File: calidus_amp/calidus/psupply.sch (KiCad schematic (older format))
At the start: 19 parts

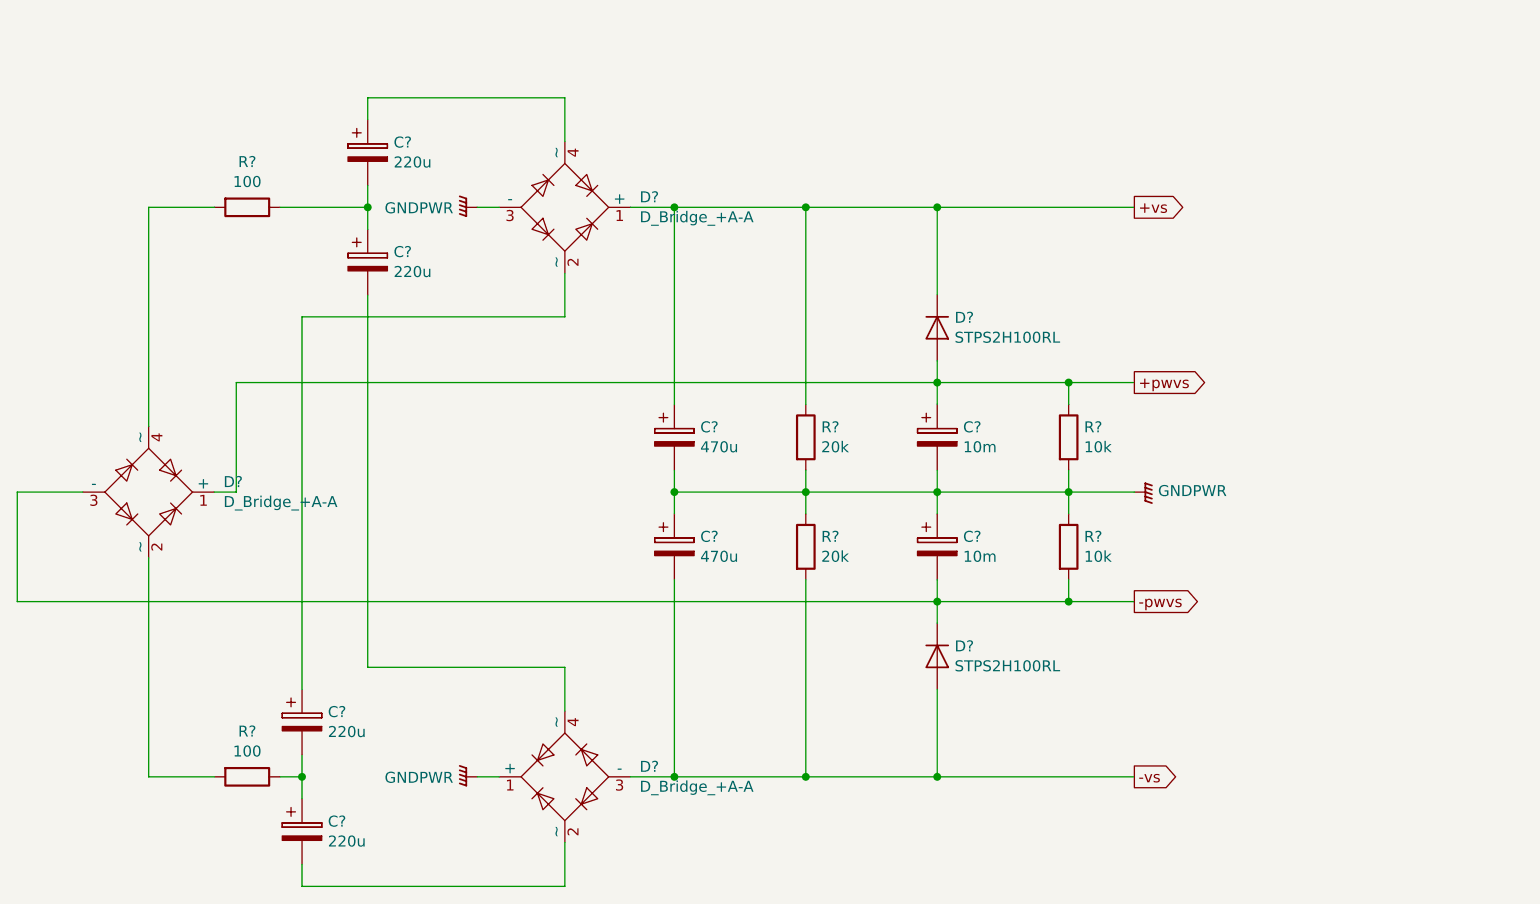
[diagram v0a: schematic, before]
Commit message: Upgraded power supply
Using new power supply design with 3pin linear regulator
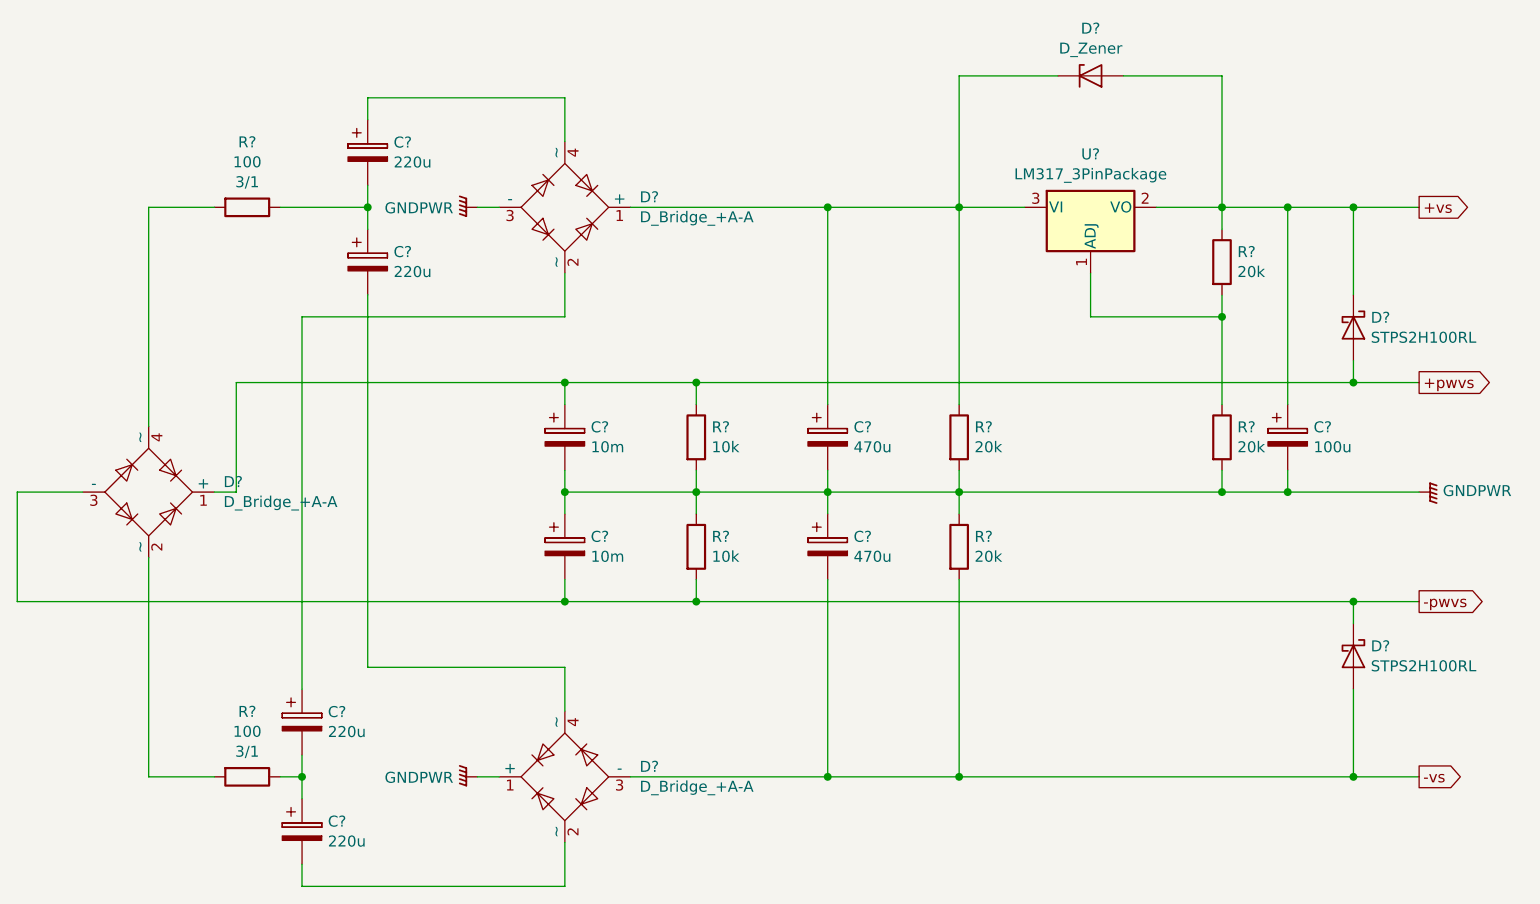
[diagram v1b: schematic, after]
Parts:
- removed D? (x2): STPS2H100RL, symbol Device:D
- removed R?: 100, symbol Device:R
- added C?: 100u, symbol Device:CP
- added D? (x2): STPS2H100RL, symbol Device:D_Schottky
- added D?: D_Zener, symbol Device:D_Zener
- added R? (x2): 20k, symbol Device:R
- added R?: 100, symbol Device:R
- added U?: LM317_3PinPackage, symbol Regulator_Linear:LM317_3PinPackage
- R?: Power (none) -> 3/1
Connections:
- net +pwvs: now also D?.2 (A)
- net +vs: now also C?.1, D?.1 (K), D?.2 (A), R?.1, U?.2 (VO); no longer C?.1, D?.1 (+), R?.1
- net -pwvs: now also D?.1 (K)
- net -vs: now also D?.2 (A)
- net GNDPWR: now also C?.2, R?.2
- net at D?.4 (~~): now also R?.2
- net at C?.1, C?.2: now also R?.1
- new net: C?.1, D?.1 (+), D?.1 (K), R?.1, U?.3 (VI)
- new net: R?.1, R?.2, U?.1 (ADJ)
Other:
- moved on the sheet: C?, R?

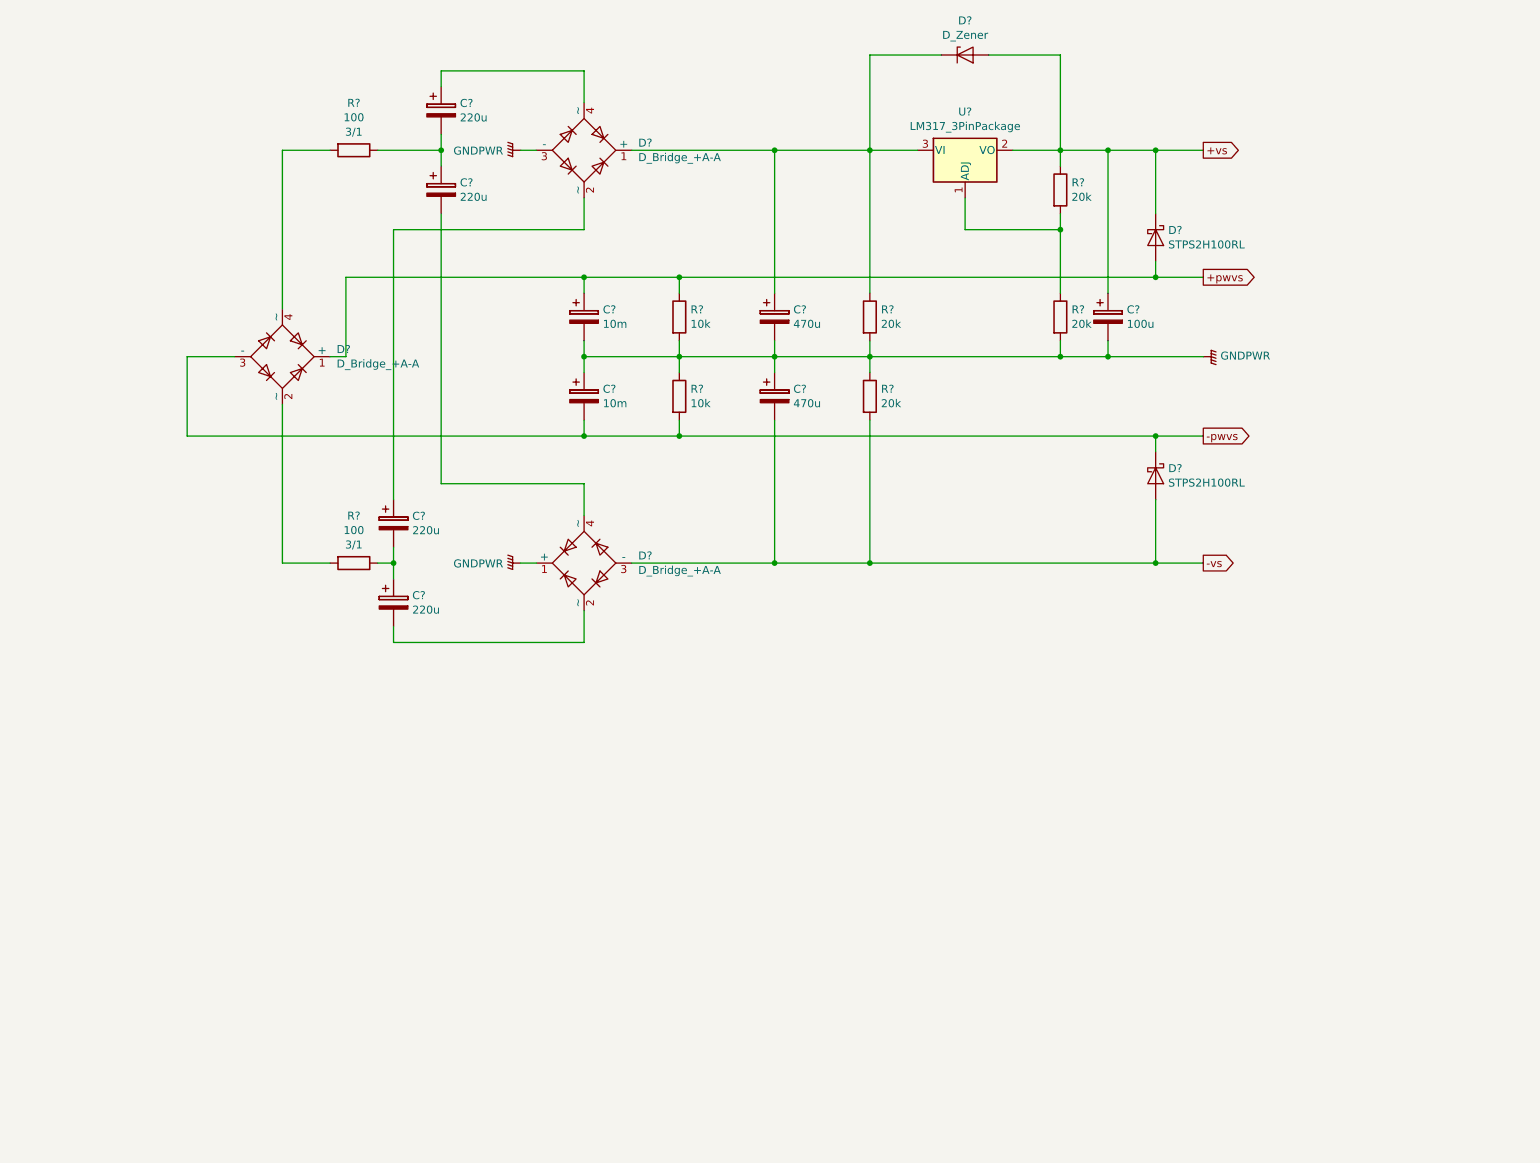
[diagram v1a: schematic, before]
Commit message: Update of the schematic
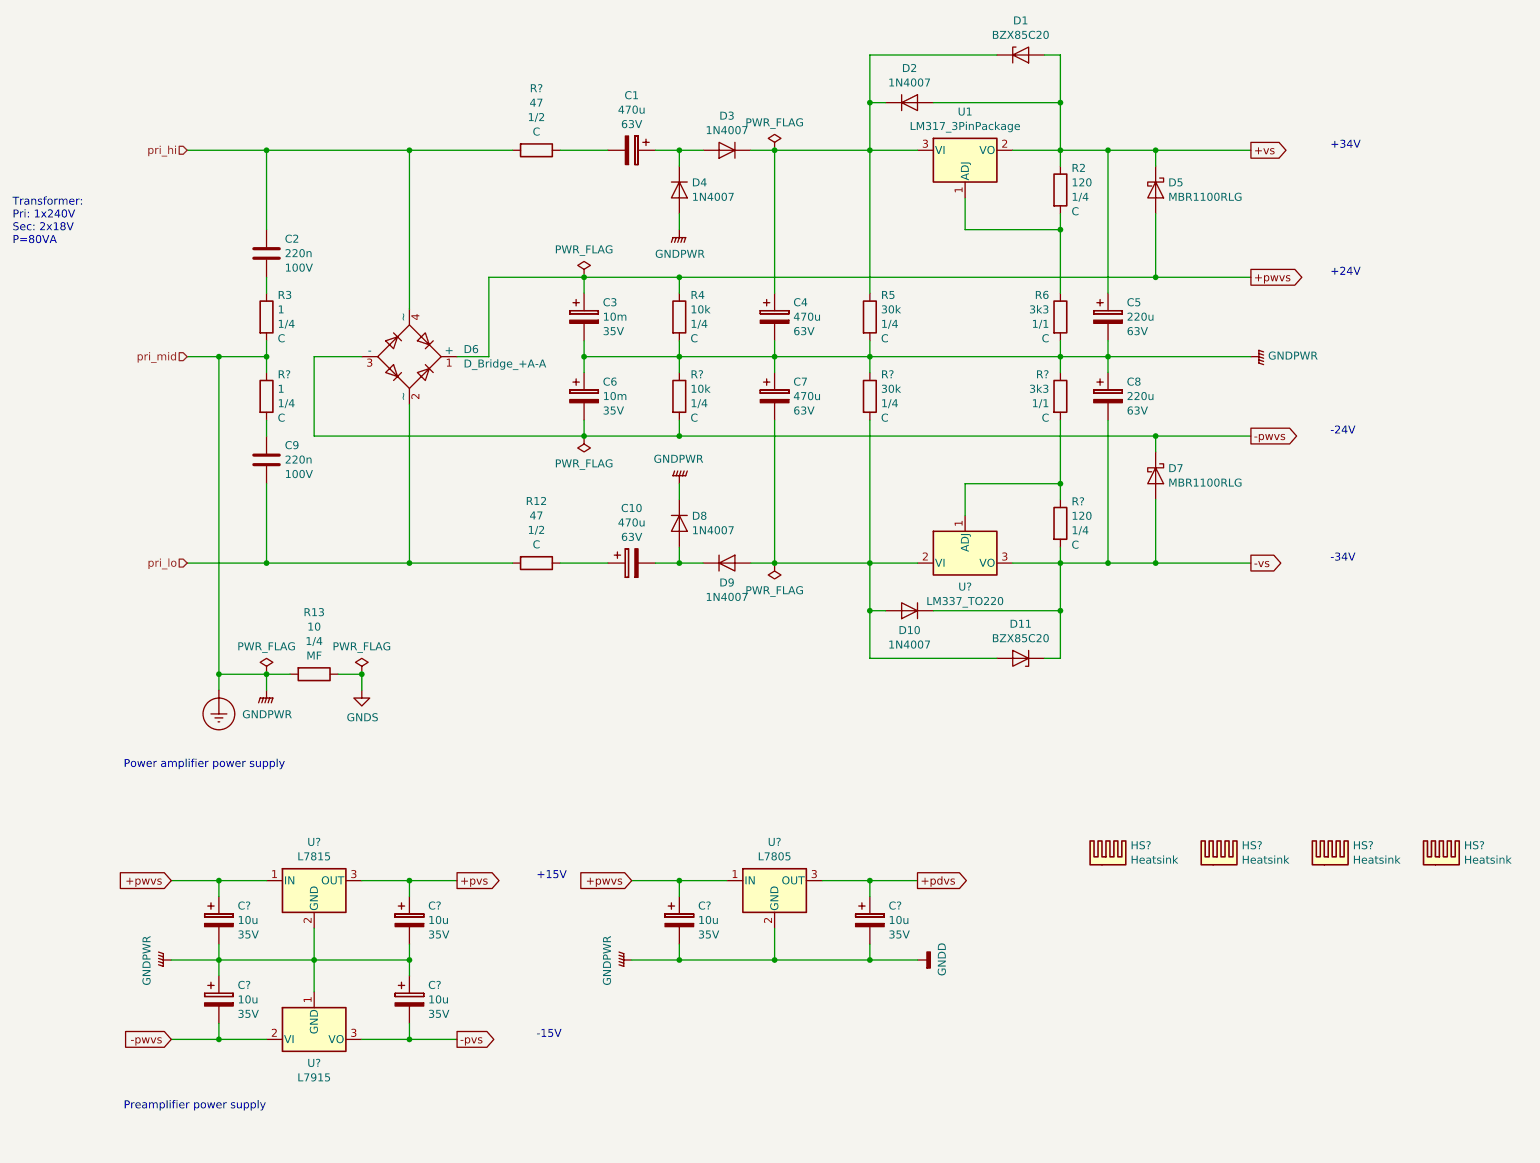
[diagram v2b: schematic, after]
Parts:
- removed C?: 10m, symbol Device:CP
- removed C? (x4): 220u, symbol Device:CP
- removed C?: 470u, symbol Device:CP
- removed C?: 100u, symbol Device:CP
- removed D? (x2): D_Bridge_+A-A, symbol Device:D_Bridge_+A-A
- removed D?: D_Zener, symbol Device:D_Zener
- removed R?: 10k, symbol Device:R
- removed R? (x3): 20k, symbol Device:R
- removed R?: 100, symbol Device:R
- removed U?: LM317_3PinPackage, symbol Regulator_Linear:LM317_3PinPackage
- added C1, C10, C7: 470u, symbol Device:CP
- added C2, C9: 220n, symbol Device:C
- added C5, C8: 220u, symbol Device:CP
- added C6: 10m, symbol Device:CP
- added C? (x6): 10u, symbol Device:CP
- added D1, D11: BZX85C20, symbol Device:D_Zener
- added D10, D2, D3, D4, D8, D9: 1N4007, symbol Device:D
- added HS? (x4): Heatsink, symbol Mechanical:Heatsink
- added R13: 10, symbol Device:R
- added R2, R?: 120, symbol Device:R
- added R3, R?: 1, symbol Device:R
- added R6, R?: 3k3, symbol Device:R
- added R?: 10k, symbol Device:R
- added R?: 47, symbol Device:R
- added R?: 30k, symbol Device:R
- added U1: LM317_3PinPackage, symbol Regulator_Linear:LM317_3PinPackage
- added U?: L7815, symbol Regulator_Linear:L7815
- added U?: L7915, symbol Regulator_Linear:L7915
- added U?: L7805, symbol Regulator_Linear:L7805
- added U?: LM337_TO220, Package_TO_SOT_THT:TO-220-3_Vertical, symbol Regulator_Linear:LM337_TO220
- C3: renamed from C?; Voltage (none) -> 35V
- C4: renamed from C?; Voltage (none) -> 63V
- D5, D7: renamed from D?; value STPS2H100RL -> MBR1100RLG
- R12: renamed from R?; value 100 -> 47; Power 3/1 -> 1/2; Type (none) -> C
- R4: renamed from R?; Power (none) -> 1/4; Type (none) -> C
- R5: renamed from R?; value 20k -> 30k; Power (none) -> 1/4; Type (none) -> C
- gave numbers to parts that had none: 1
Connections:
- net +pwvs: now also C?.1, C?.1, U?.1 (IN), U?.1 (IN)
- net +vs: now also C5.1, D1.2 (A), D2.2 (A), R2.1, U1.2 (VO)
- net -pwvs: now also C6.2, C?.2, R?.2, U?.2 (VI)
- net -vs: now also C8.2, D10.1 (K), D11.1 (K), R?.2, U?.3 (VO)
- net pri_lo: now reaches D6.2 (~~), R12.2
- net pri_lo: now also C9.2
- net pri_hi: now reaches D6.4 (~~)
- net pri_hi: now also C2.1, R?.2
- net at C4.1, R5.1: now also D1.1 (K), D2.1 (K), D3.1 (K), U1.3 (VI)
- net at R12.1: now also C10.1
- net GNDPWR renamed Earth_Protective
- net Earth_Protective: now also C5.2, C6.1, C7.1, C8.1, C?.1, C?.1, C?.2, C?.2, C?.2, C?.2, D4.2 (A), D8.1 (K), R13.2, R3.2, R6.2, R?.1, R?.1, R?.1, R?.1, U?.1 (GND), U?.2 (GND), U?.2 (GND)
- new net: C7.2, D10.2 (A), D11.2 (A), D9.2 (A), R?.2, U?.2 (VI)
- new net: C1.1, D3.2 (A), D4.1 (K)
- new net: C9.1, R?.2
- new net: R?.1, R?.2, U?.1 (ADJ)
- new net: C1.2, R?.1
- new net: C10.2, D8.2 (A), D9.1 (K)
- new net: R2.2, R6.1, U1.1 (ADJ)
- new net: C2.2, R3.1
- new net +pdvs: C?.1, U?.3 (OUT)
- new net +pvs: C?.1, U?.3 (OUT)
- new net -pvs: C?.2, U?.3 (VO)
- new net GNDS: R13.1
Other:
- note added: "+15V"
- note added: "+24V"
- note added: "+34V"
- note added: "-15V"
- note added: "-24V"
- note added: "-34V"
- note added: "Power amplifier power supply"
- note added: "Preamplifier power supply"
- note added: "Transformer:\nPri: 1x240V\nSec: 2x18V\nP=80VA"
- moved on the sheet: D5, D6, R12

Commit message: Updated component designators and finished CMU
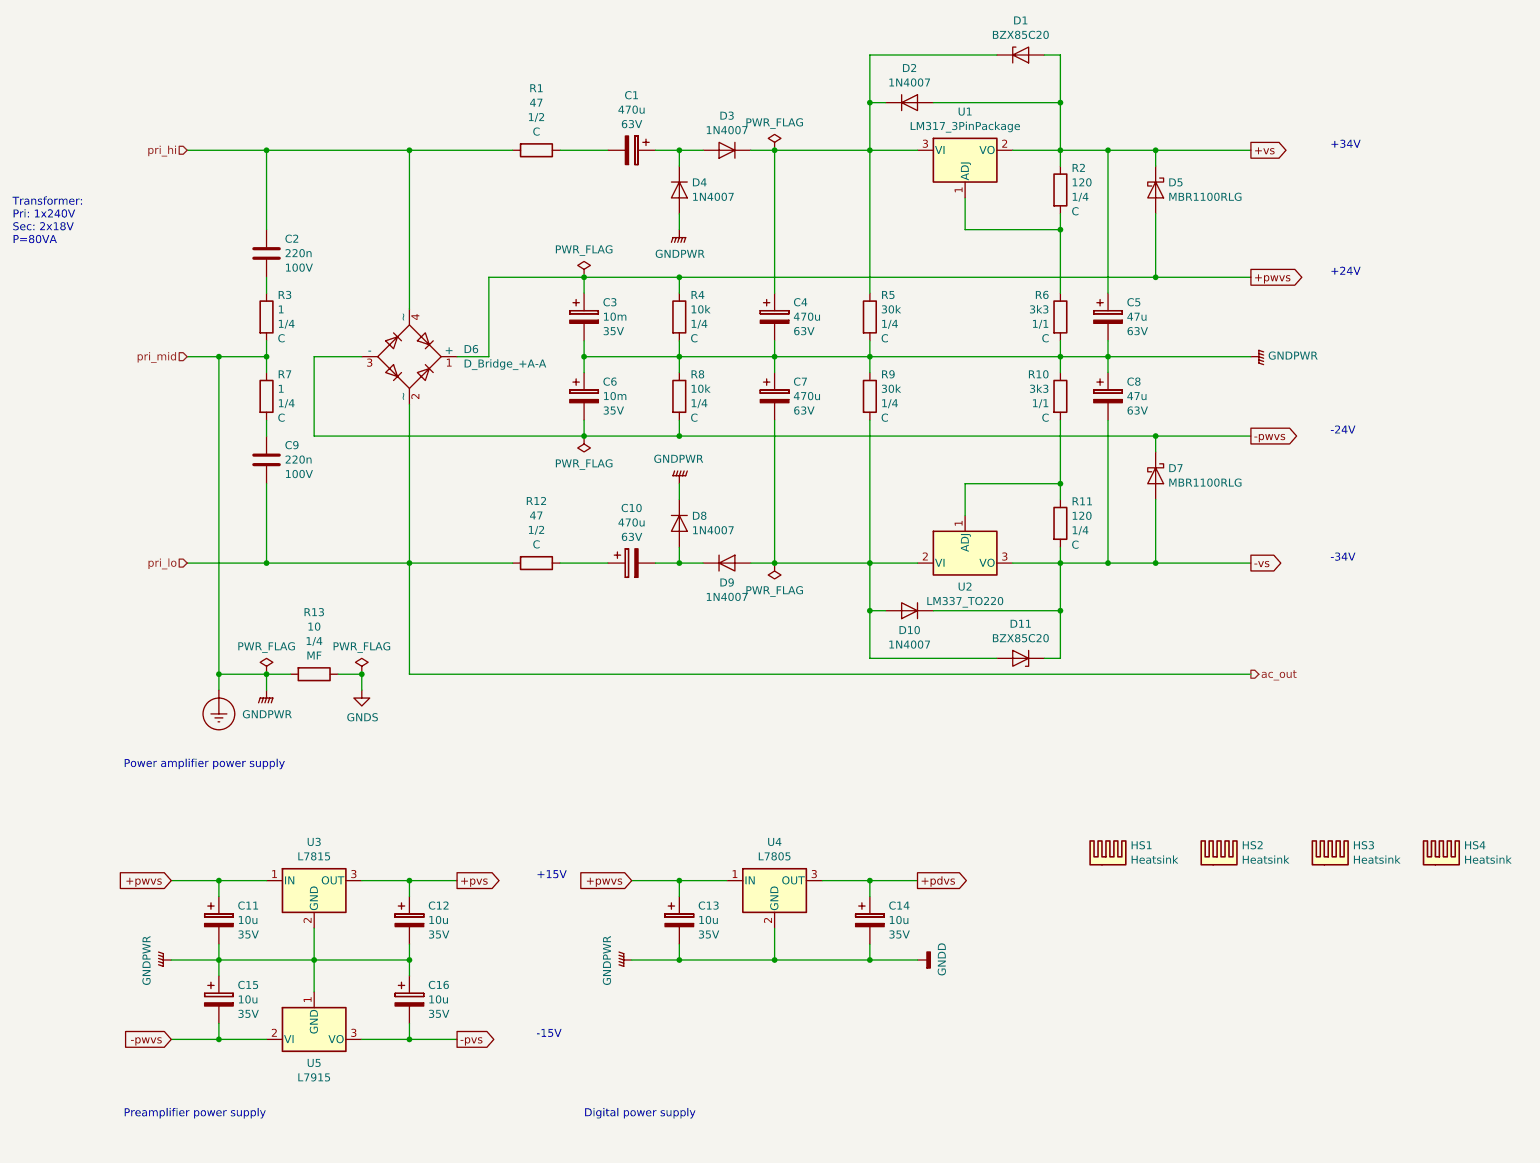
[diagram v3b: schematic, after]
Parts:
- C5, C8: value 220u -> 47u
- HS1, HS2, HS3, HS4: renamed from HS?; footprint (none) -> Heatsink:Heatsink_Fischer_SK104-STCB_35x13mm__2xDrill3.5mm_ScrewM3
- U1: footprint (none) -> Package_TO_SOT_THT:TO-220-3_Vertical
- U3, U4, U5: renamed from U?; footprint (none) -> Package_TO_SOT_THT:TO-220-3_Vertical
- gave numbers to parts that had none: 13
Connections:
- net pri_lo renamed ac_out
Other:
- note added: "Digital power supply"
